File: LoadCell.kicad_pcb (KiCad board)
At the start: 2 copper layers, 51.1 x 38.1 mm, 83 parts, among them J1 M20-8760242, J10 M20-8760242, J11 0.100_1X4, J12 0.100_1X4, J13 M20-8760242, J14 M20-8760242, J15 0.100_1X4, J16 0.100_1X4, J2 M20-8760242, J3 0.100_1X4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

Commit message: Parts placed
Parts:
- moved R17 62.4 mm to (110.0, 91.2), turned to 90 degrees
- moved R18 61.9 mm to (104.6, 91.2), turned to 90 degrees
- moved R19 56.4 mm to (123.2, 91.2), turned to 90 degrees
- moved R20 54.8 mm to (117.9, 91.2), turned to 90 degrees
- moved R21 54.8 mm to (108.2, 91.2), turned to 270 degrees
- moved D8 54.2 mm to (151.6, 95.5), turned to 270 degrees
- moved R22 53.7 mm to (106.4, 91.2), turned to 270 degrees
- moved C11 51.9 mm to (102.7, 91.2), turned to 90 degrees
- moved C9 51.1 mm to (111.8, 91.2), turned to 270 degrees
- moved R23 48.5 mm to (121.4, 91.2), turned to 270 degrees
- moved D7 48.0 mm to (138.3, 95.3), turned to 270 degrees
- moved D4 47.4 mm to (151.6, 75.8), turned to 270 degrees
- moved R27 47.4 mm to (149.6, 91.2), turned to 90 degrees
- moved D5 47.1 mm to (112.0, 95.4), turned to 270 degrees
- moved R24 46.6 mm to (119.6, 91.2), turned to 270 degrees
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
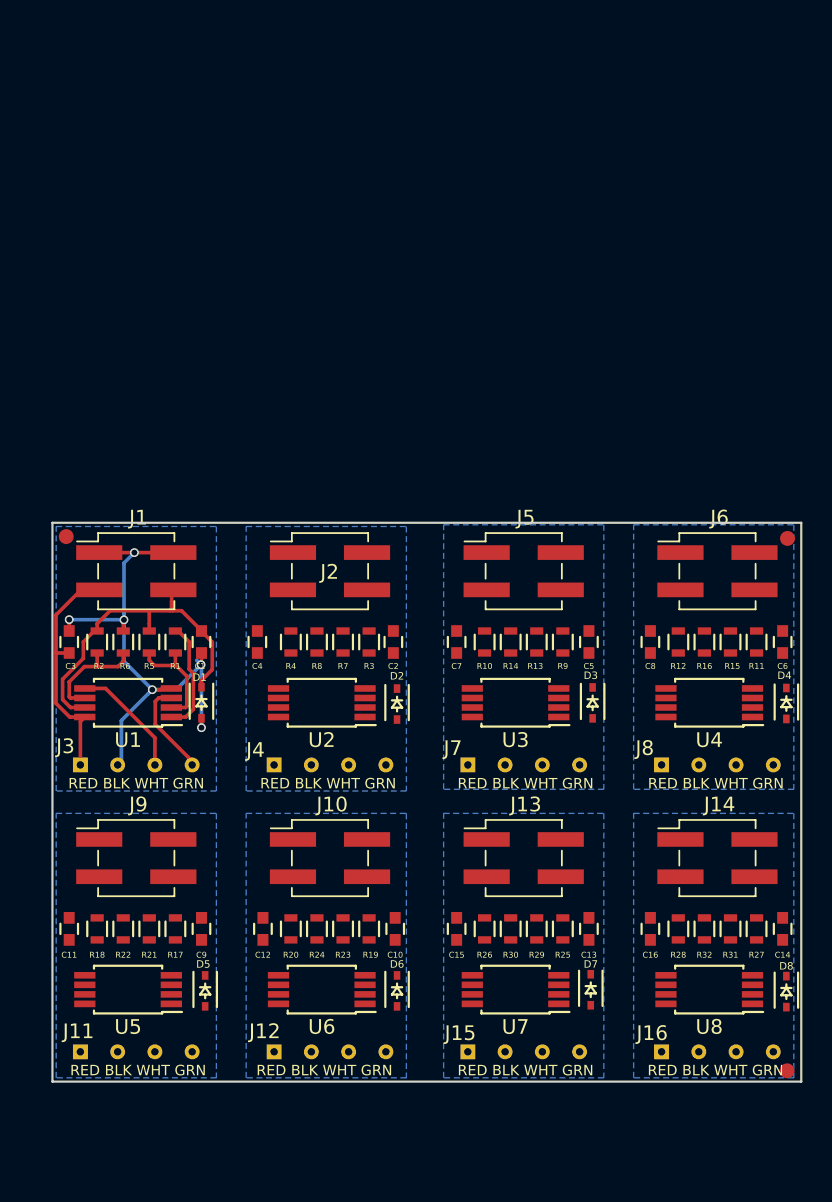
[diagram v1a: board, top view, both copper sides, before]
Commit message: Fully routed panel of 8 adapters
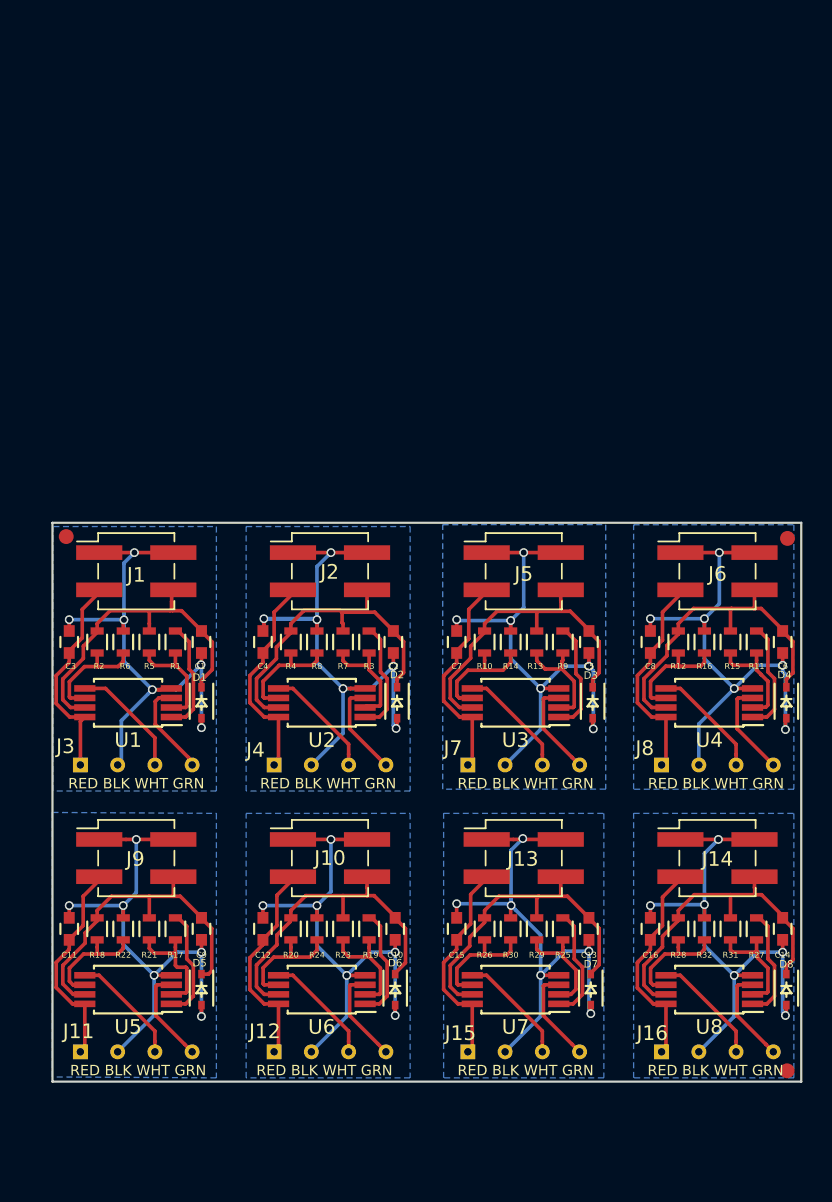
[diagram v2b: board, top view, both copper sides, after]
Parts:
- moved C4 0.38 mm to (116.0, 71.6)
- moved D5 0.27 mm to (111.8, 95.3)
- moved D6 0.16 mm to (125.0, 95.3)
- moved D8 0.14 mm to (151.6, 95.3)
- moved D2 0.09 mm to (125.1, 75.8)
- moved D4 0.05 mm to (151.6, 75.8)
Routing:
- net Net-(C2-Pad2): track 0.00 -> 41.7 mm, vias 0 -> 6
- net Net-(C6-Pad2): track 0.00 -> 38.5 mm, vias 0 -> 6
- net Net-(C14-Pad2): track 0.00 -> 38.4 mm, vias 0 -> 6
- net Net-(C11-Pad2): track 0.00 -> 38.4 mm, vias 0 -> 6
- net Net-(C13-Pad2): track 0.00 -> 38.3 mm, vias 0 -> 6
- net Net-(C10-Pad2): track 0.00 -> 38.2 mm, vias 0 -> 6
- net Net-(C5-Pad2): track 0.00 -> 38.1 mm, vias 0 -> 6
- net Net-(C10-Pad1): track 0.00 -> 23.5 mm
- net Net-(C9-Pad1): track 0.00 -> 23.4 mm
- net Net-(C6-Pad1): track 0.00 -> 23.3 mm
- net Net-(C13-Pad1): track 0.00 -> 23.3 mm
- net Net-(C14-Pad1): track 0.00 -> 23.2 mm
- net Net-(C5-Pad1): track 0.00 -> 23.0 mm
- net Net-(C2-Pad1): track 0.00 -> 23.0 mm
- net Net-(C12-Pad1): track 0.00 -> 14.7 mm
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- added copper zone on B.Cu, net Net-(C10-Pad2)
- added copper zone on B.Cu, net Net-(C11-Pad2)
- added copper zone on B.Cu, net Net-(C13-Pad2)
- added copper zone on B.Cu, net Net-(C14-Pad2)
- added copper zone on B.Cu, net Net-(C2-Pad2)
- added copper zone on B.Cu, net Net-(C5-Pad2)
- added copper zone on B.Cu, net Net-(C6-Pad2)
- removed copper zone on B.Cu, net GND

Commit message: Update before generating project outputs
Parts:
- moved C2 0.13 mm to (125.0, 71.6)
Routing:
- net Net-(C2-Pad2): track 41.7 -> 38.6 mm
- net Net-(C4-Pad1): track 14.7 -> 15.3 mm
- net Net-(C2-Pad1): track 23.0 -> 23.5 mm
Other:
- board text added: "+5v"
- board text added: "Vout"
- board text added: "Vout GND"
